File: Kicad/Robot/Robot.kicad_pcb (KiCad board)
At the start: 2 copper layers, 26 parts, among them J1 X8R HEADER, J10 LightBar1, J11 LightBar2, J2 LORA, J3 RELAY HEADER, J4 SENSOR 1, J5 SENSOR 2, J6 SENSOR 3, J7 SENSOR 4, J8 MotorDriver1, J9 MotorDriver2, U1 USB_POWER, U2 Generic_DC_to_DC_Module, U3 Generic_DC_to_DC_Module, U4 Generic_DC_to_DC_Module, U5 Generic_DC_to_DC_Module, U6 X8R_Receiver, U7 TBD62089A, U8 RFM9X

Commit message: UPDATED PARTS ON PCB
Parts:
- added J12: PIN HEADER DE0-NANO POWER, Robot:PinHeader_1x02_P2.54mm_Vertical, F.Cu at (64.3, -18.5)
- added JP3: Jumper, Robot:PinHeader_1x02_P2.54mm_Vertical, F.Cu at (64.3, -11.3)
- added R5: 4.7K, Robot:R_Axial_DIN0204_L3.6mm_D1.6mm_P5.08mm_Vertical, F.Cu at (54.6, -5.08)
- added U7: TXS0108E, Robot:TSSOP-20_4.4x6.5mm_P0.65mm, F.Cu at (44.5, -3.81)
- added U9: TDB62381A, Robot:SOIC-18W_7.5x11.6mm_P1.27mm, F.Cu at (45.7, -15.2)
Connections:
- net /PWR_DE0_NANO renamed Net-(J12-Pad1)
- JP2 pad 29: Net-(JP2-Pad29) -> /VCC3P3
- U2 pad 3: Net-(J10-Pad3) -> Net-(JP3-Pad2)
- U2 pad 4: Net-(J10-Pad3) -> Net-(JP3-Pad2)
- U6 pad 1: Net-(JP2-Pad14) -> Net-(U6-Pad1)
- U6 pad 2: Net-(JP2-Pad16) -> Net-(U6-Pad2)
- U6 pad 3: Net-(JP2-Pad18) -> Net-(U6-Pad3)
- U6 pad 4: Net-(JP2-Pad20) -> Net-(U6-Pad4)
- U6 pad 5: Net-(JP2-Pad22) -> Net-(U6-Pad5)
- U6 pad 6: Net-(JP2-Pad24) -> Net-(U6-Pad6)
- U6 pad 7: Net-(JP2-Pad26) -> Net-(U6-Pad7)
- U6 pad 8: Net-(JP2-Pad28) -> Net-(U6-Pad8)
- U8 pad 1: Net-(U8-Pad1) -> /PWR_X8R

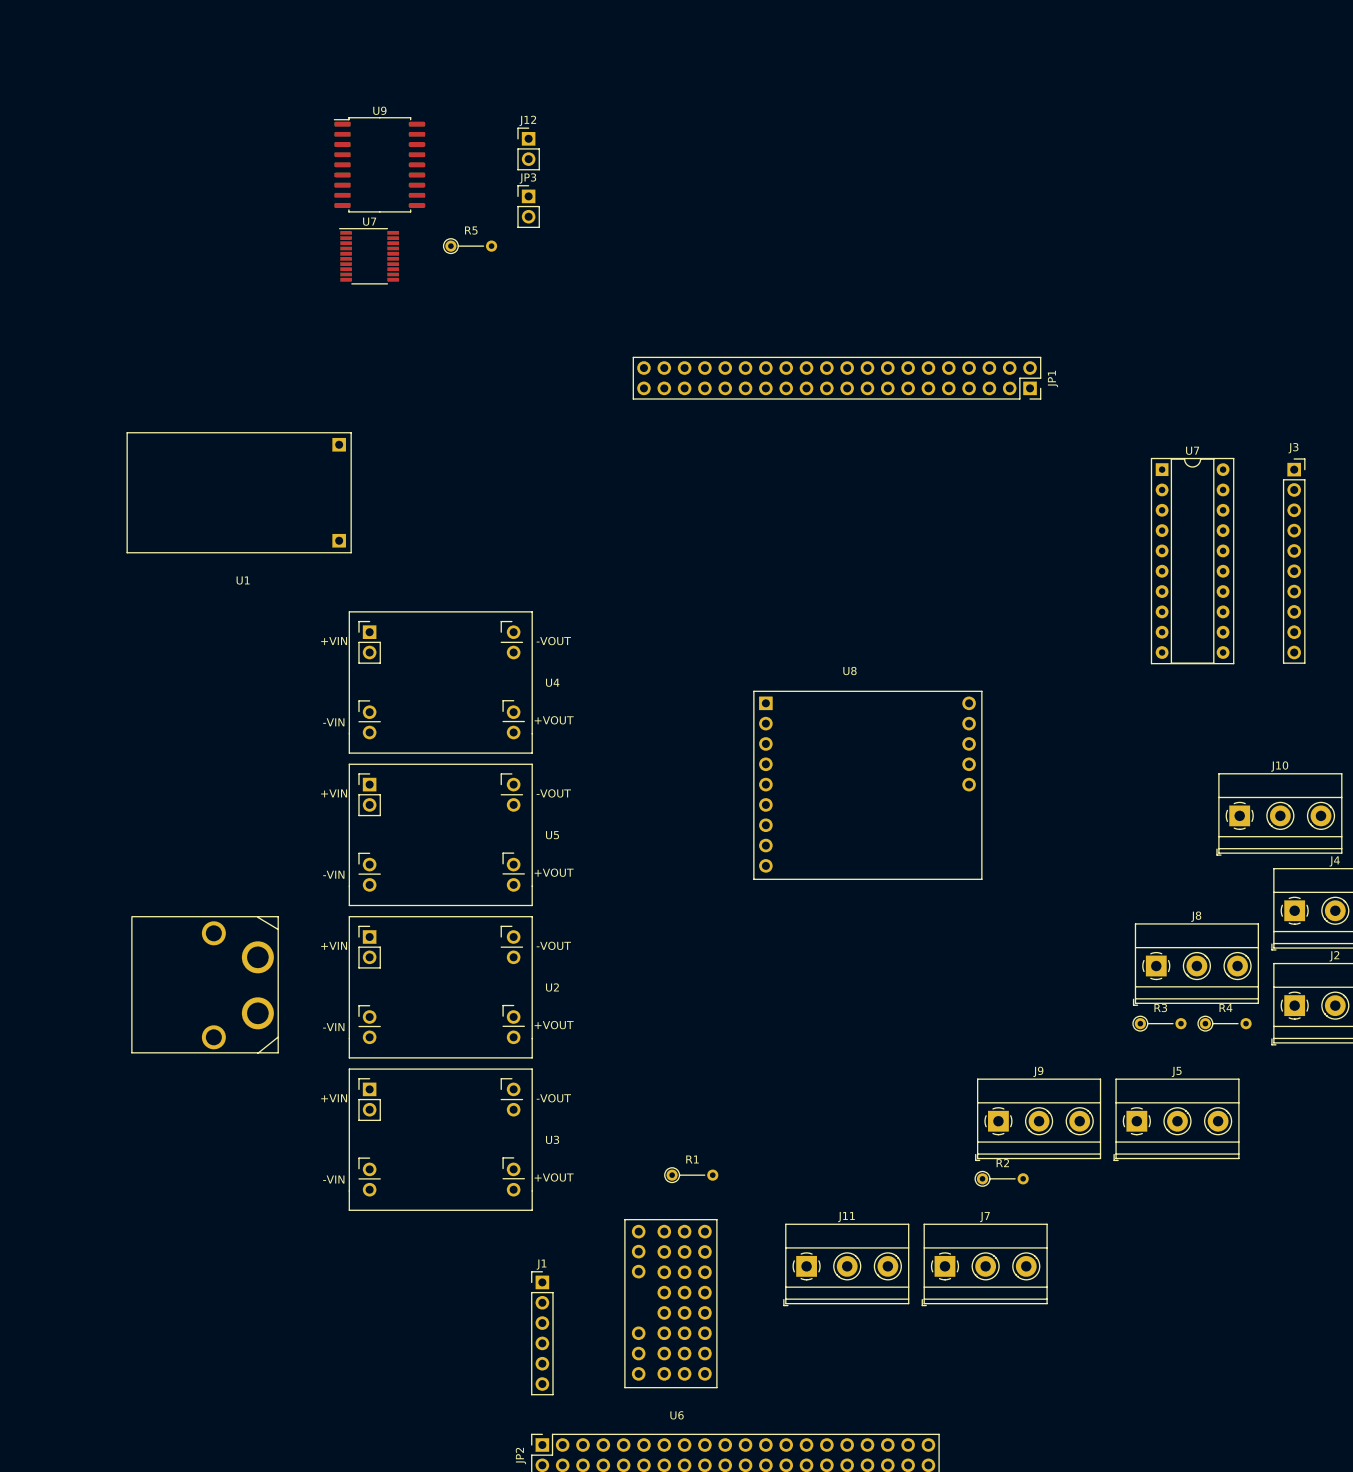
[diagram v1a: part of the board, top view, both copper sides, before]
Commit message: add decoupling caps
added decoupling caps
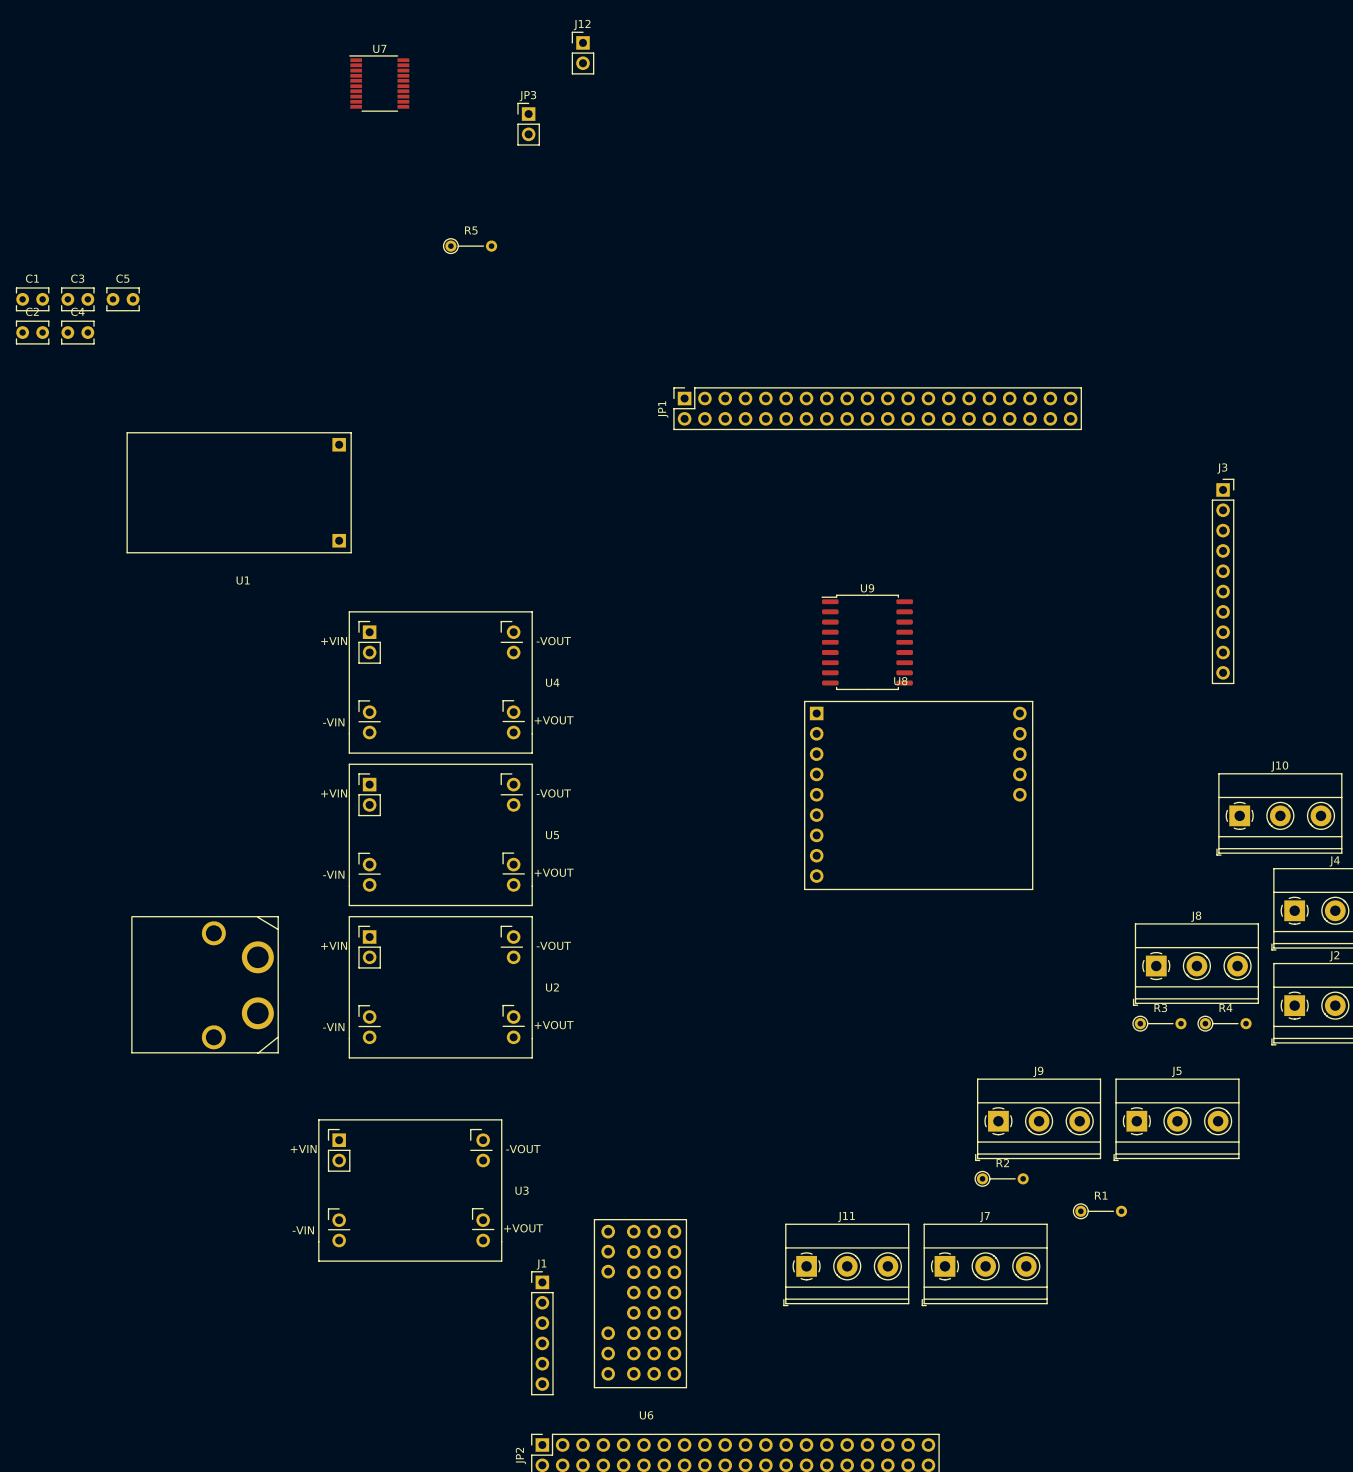
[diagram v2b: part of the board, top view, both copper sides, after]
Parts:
- removed the U7 at (143.5, 22.9)
- added C1: .1uf, Robot:C_Disc_D3.8mm_W2.6mm_P2.50mm, F.Cu at (1.08, 1.58)
- added C2: .1uf, Robot:C_Disc_D3.8mm_W2.6mm_P2.50mm, F.Cu at (1.08, 5.73)
- added C3: .1uf, Robot:C_Disc_D3.8mm_W2.6mm_P2.50mm, F.Cu at (6.73, 1.58)
- added C4: .1uf, Robot:C_Disc_D3.8mm_W2.6mm_P2.50mm, F.Cu at (6.73, 5.73)
- added C5: .1uf, Robot:C_Disc_D3.8mm_W2.6mm_P2.50mm, F.Cu at (12.4, 1.58)
- moved U9 85.3 mm to (106.7, 44.5)
- moved R1 51.3 mm to (133.3, 115.6)
- moved JP1 43.2 mm to (83.8, 14.0), turned to 90 degrees
- moved U7 21.6 mm to (45.7, -25.4)
- moved J12 13.8 mm to (71.1, -30.5)
- moved JP3 10.3 mm to (64.3, -21.6)
- moved J3 9.25 mm to (151.1, 25.4)
- moved U3 7.41 mm to (40.6, 106.7)
- moved U8 6.48 mm to (100.3, 53.3)
- moved U6 3.81 mm to (82.5, 118.1)

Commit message: add sip resistor
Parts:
- added RN1: R_Network04, Robot:R_Array_SIP5, F.Cu at (158.8, 120.7)
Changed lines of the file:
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@@
     (tracks 0)
     (zones 0)
-    (modules 35)
+    (modules 36)
     (nets 118)
   )
@@
     (add_net "Net-(U8-Pad14)")
   )
+  (module Robot:R_Array_SIP5 (layer F.Cu)
+    (at 158.75 120.65)
+    (descr "5-pin Resistor SIP pack")
+    (tags R)
+    (fp_text reference RN1 (at 6.35 -2.4) (layer F.SilkS)
+      (effects (font (size 1 1) (thickness 0.15)))
+    )
+    (fp_text value R_Network04 (at 6.35 2.4) (layer F.Fab)
+      (effects (font (size 1 1) (thickness 0.15)))
+    )
+    (fp_line (start 11.9 -1.65) (end -1.7 -1.65) (layer F.CrtYd) (width 0.05))
+    (fp_line (start 11.9 1.65) (end 11.9 -1.65) (layer F.CrtYd) (width 0.05))
+    (fp_line (start -1.7 1.65) (end 11.9 1.65) (layer F.CrtYd) (width 0.05))
+    (fp_line (start -1.7 -1.65) (end -1.7 1.65) (layer F.CrtYd) (width 0.05))
+    (fp_line (start 1.27 -1.4) (end 1.27 1.4) (layer F.SilkS) (width 0.12))
+    (fp_line (start 11.6 -1.4) (end -1.44 -1.4) (layer F.SilkS) (width 0.12))
+    (fp_line (start 11.6 1.4) (end 11.6 -1.4) (layer F.SilkS) (width 0.12))
+    (fp_line (start -1.44 1.4) (end 11.6 1.4) (layer F.SilkS) (width 0.12))
+    (fp_line (start -1.44 -1.4) (end -1.44 1.4) (layer F.SilkS) (width 0.12))
+    (fp_line (start 1.27 -1.25) (end 1.27 1.25) (layer F.Fab) (width 0.1))
+    (fp_line (start 11.45 -1.25) (end -1.29 -1.25) (layer F.Fab) (width 0.1))
+    (fp_line (start 11.45 1.25) (end 11.45 -1.25) (layer F.Fab) (width 0.1))
+    (fp_line (start -1.29 1.25) (end 11.45 1.25) (layer F.Fab) (width 0.1))
+    (fp_line (start -1.29 -1.25) (end -1.29 1.25) (layer F.Fab) (width 0.1))
+    (fp_text user %R (at 5.08 0) (layer F.Fab)
+      (effects (font (size 1 1) (thickness 0.15)))
+    )
+    (pad 5 thru_hole oval (at 10.16 0) (size 1.6 1.6) (drill 0.8) (layers *.Cu *.Mask)
+      (net 23 "Net-(J7-Pad2)"))
+    (pad 4 thru_hole oval (at 7.62 0) (size 1.6 1.6) (drill 0.8) (layers *.Cu *.Mask)
+      (net 22 "Net-(J6-Pad2)"))
+    (pad 3 thru_hole oval (at 5.08 0) (size 1.6 1.6) (drill 0.8) (layers *.Cu *.Mask)
+      (net 21 "Net-(J5-Pad2)"))
+    (pad 2 thru_hole oval (at 2.54 0) (size 1.6 1.6) (drill 0.8) (layers *.Cu *.Mask)
+      (net 19 "Net-(J4-Pad2)"))
+    (pad 1 thru_hole rect (at 0 0) (size 1.6 1.6) (drill 0.8) (layers *.Cu *.Mask)
+      (net 39 /3v_pullup))
+    (model ${KISYS3DMOD}/Resistor_THT.3dshapes/R_Array_SIP5.wrl
+      (at (xyz 0 0 0))
+      (scale (xyz 1 1 1))
+      (rotate (xyz 0 0 0))
+    )
+  )
   (module Robot:RFM9X (layer F.Cu)

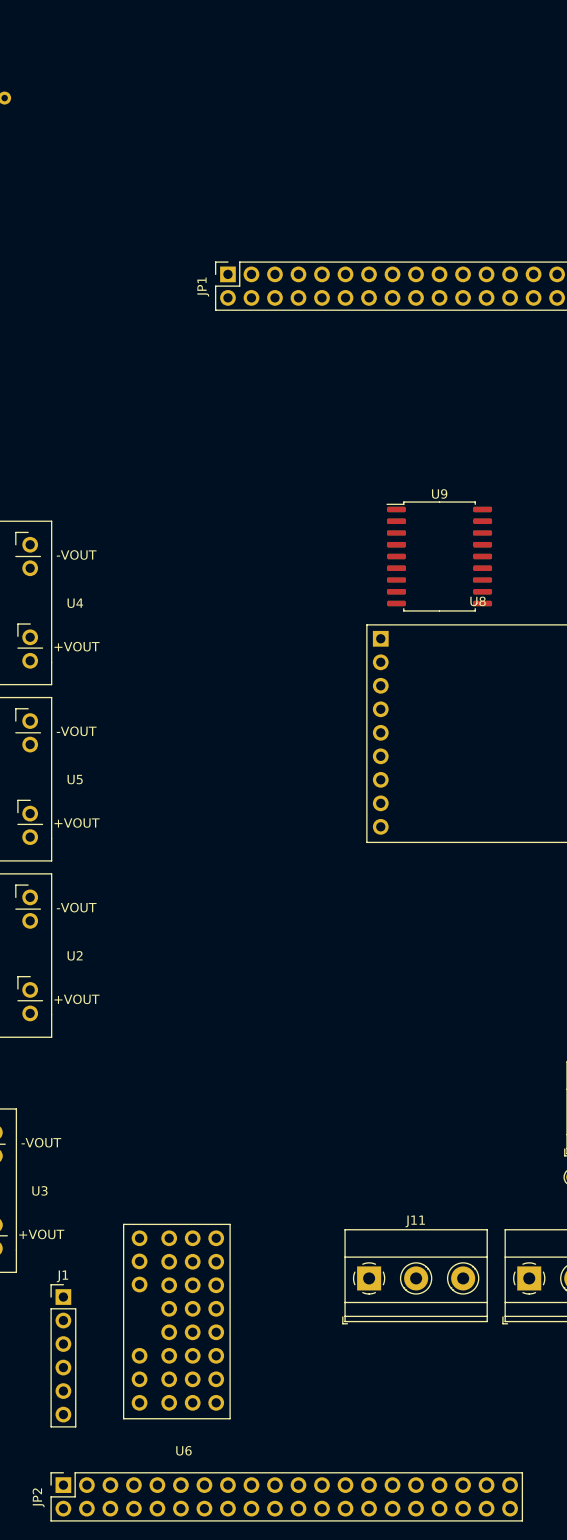
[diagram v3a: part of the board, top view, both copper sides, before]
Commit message: updates 2x20 header decal
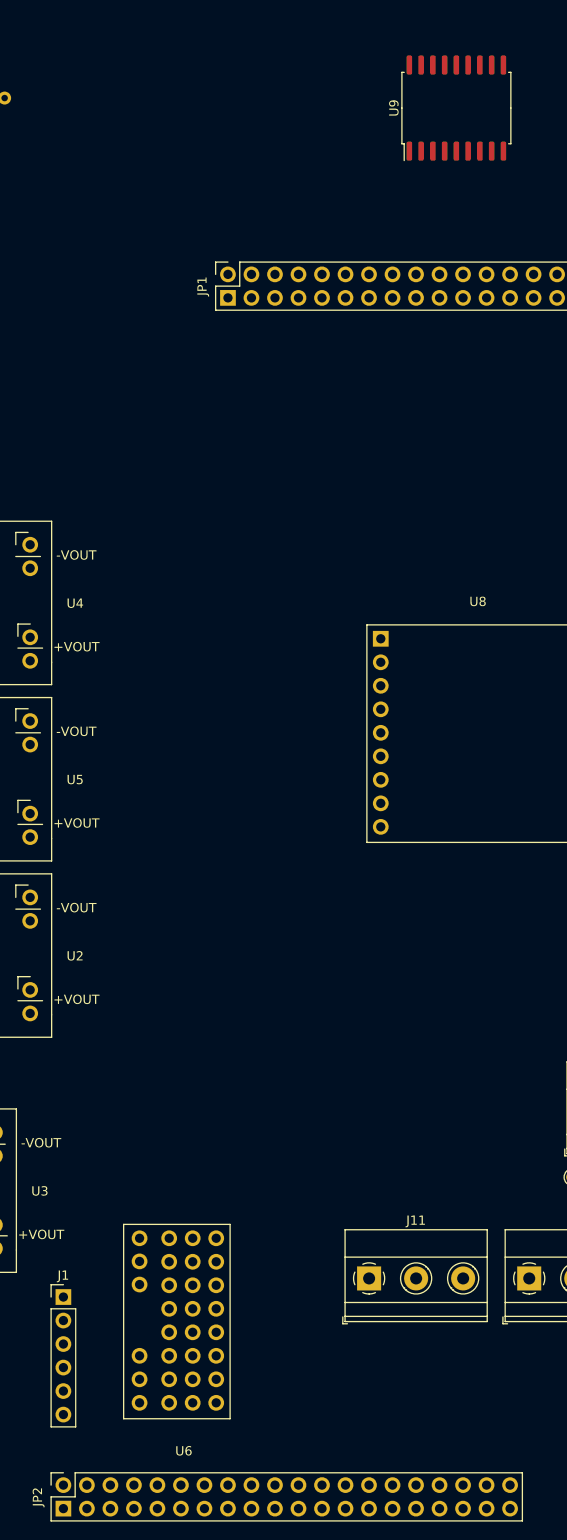
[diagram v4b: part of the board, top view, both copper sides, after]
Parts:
- moved U9 48.5 mm to (108.5, -4.00), turned to 90 degrees
